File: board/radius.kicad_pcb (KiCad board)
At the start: 2 copper layers, 25.4 x 12.1 mm, 11 parts, among them IC1 STM8S003F3P, P1 CONN_01X04, P2 CONN_01X10, U1 CH340G, U2 LM2931AZ-3.3/5.0, Y1 Crystal

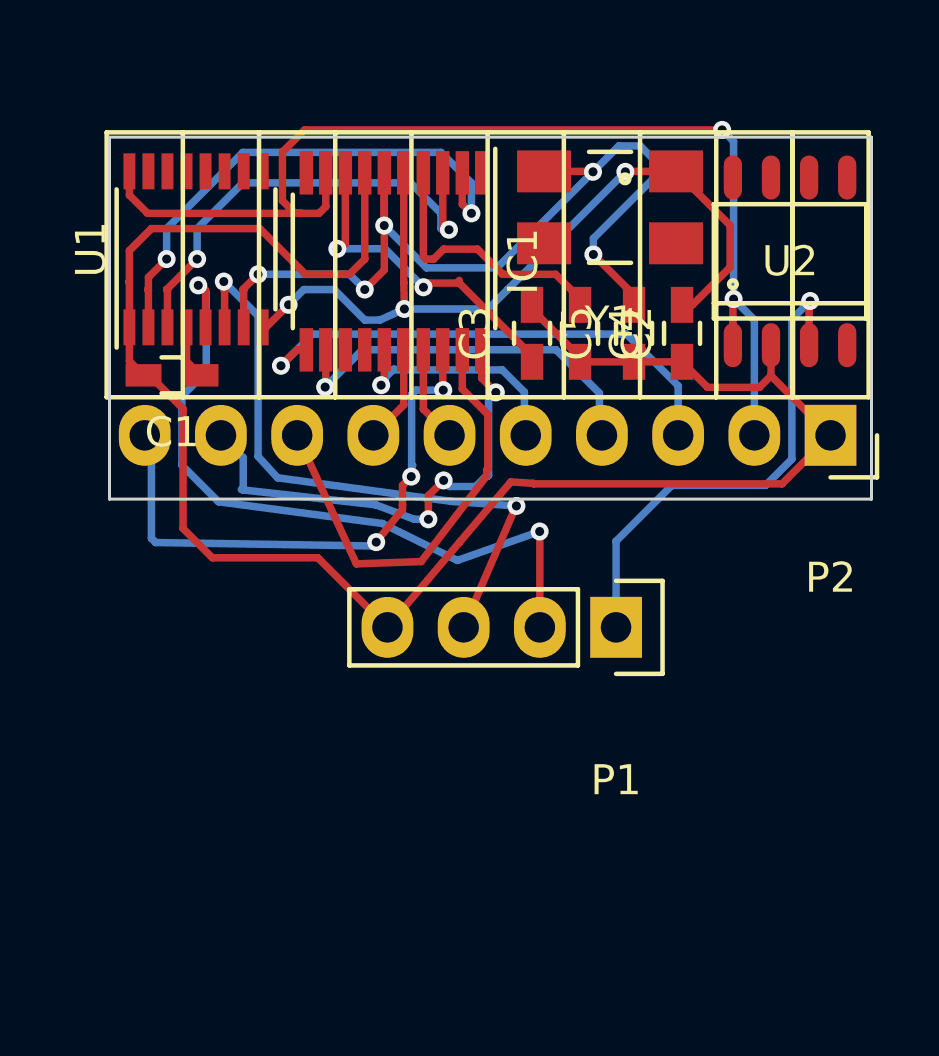
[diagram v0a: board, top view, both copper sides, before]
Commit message: Cleans up upper components.
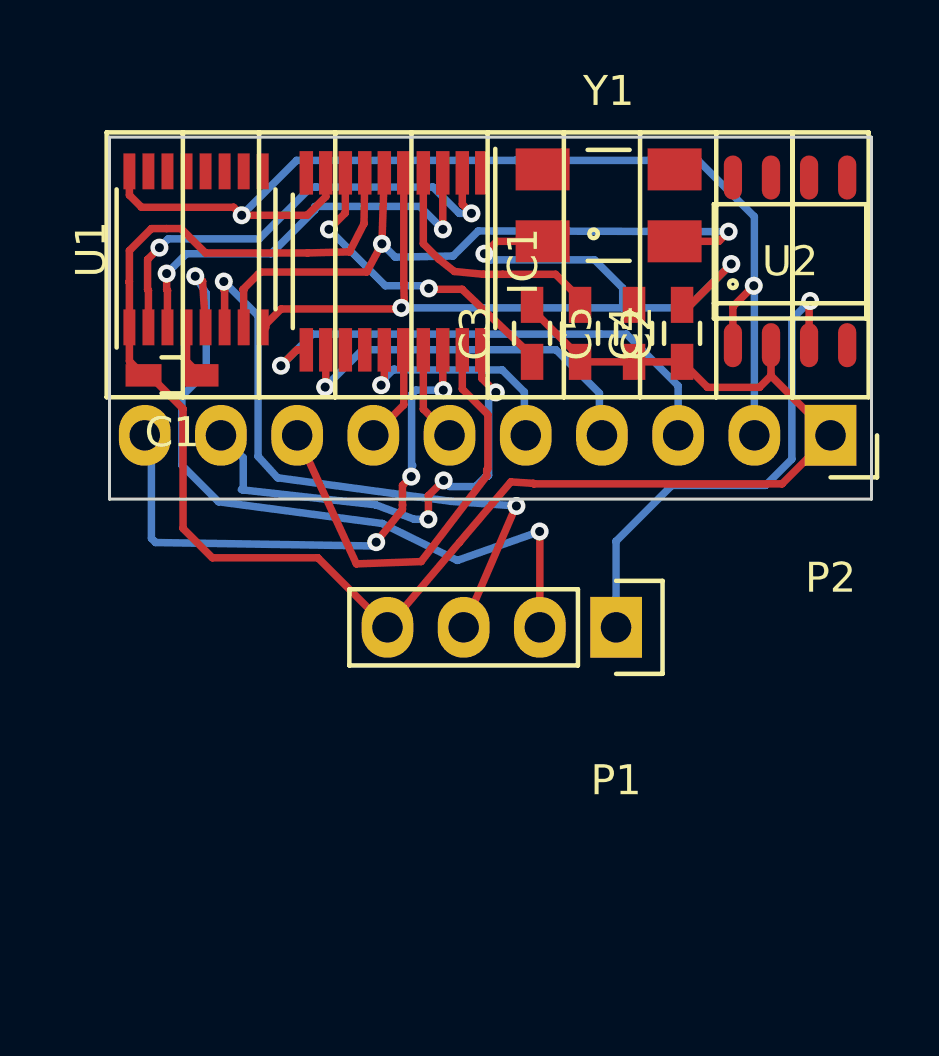
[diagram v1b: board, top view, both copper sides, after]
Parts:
- moved Y1 0.08 mm to (149.4, 101.3), turned to 0 degrees
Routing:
- net XI: track 31.1 -> 23.4 mm, vias 5 -> 2
- net XO: track 27.3 -> 31.4 mm
- net USB_TX: track 17.7 -> 15.9 mm
- net USB_RX: track 15.8 -> 14.2 mm
- net GND: track 61.1 -> 59.9 mm
- net VCC: track 39.1 -> 38.0 mm
- net Net-(C2-Pad1): track 9.20 -> 8.52 mm
- net D+: track 24.2 -> 24.8 mm

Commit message: Qualifying layout
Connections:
- IC1 pad 14: Net-(IC1-Pad14) -> G3
- IC1 pad 18: G3 -> Net-(IC1-Pad18)
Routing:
- net G3: track 19.0 -> 12.7 mm, vias 3 -> 1
- net D-: track 21.2 -> 16.7 mm
- net D+: track 24.8 -> 20.3 mm, vias 2 -> 1
- net TXD: track 15.0 -> 18.7 mm, vias 0 -> 3
- net XI: track 23.4 -> 26.4 mm
- net XO: track 31.4 -> 29.3 mm, vias 3 -> 4
- net SDA: track 17.1 -> 19.1 mm
- net Net-(C3-Pad1): track 10.8 -> 12.6 mm
- net SCK: track 8.09 -> 9.02 mm
- net SCL: track 12.9 -> 13.6 mm
- net GND: track 59.9 -> 60.6 mm
- net USB_TX: track 15.9 -> 16.6 mm
- net USB_RX: track 14.2 -> 14.8 mm
- net RXD: track 16.5 -> 16.4 mm, vias 3 -> 1

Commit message: Redone
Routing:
- net TXD: track 18.7 -> 14.0 mm, vias 3 -> 1
- net VCC: track 38.0 -> 42.1 mm
- net G3: track 12.7 -> 14.9 mm
- net SCK: track 9.02 -> 7.15 mm
- net XO: track 29.3 -> 27.5 mm
- net D-: track 16.7 -> 15.2 mm, vias 2 -> 0
- net SCL: track 13.6 -> 15.0 mm
- net RXD: track 16.4 -> 15.2 mm
- net USB_TX: track 16.6 -> 15.6 mm
- net D+: track 20.3 -> 19.7 mm
- net GND: track 60.6 -> 60.1 mm, vias 0 -> 1
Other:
- board size 25.4 x 12.1 mm -> 25.4 x 28.6 mm

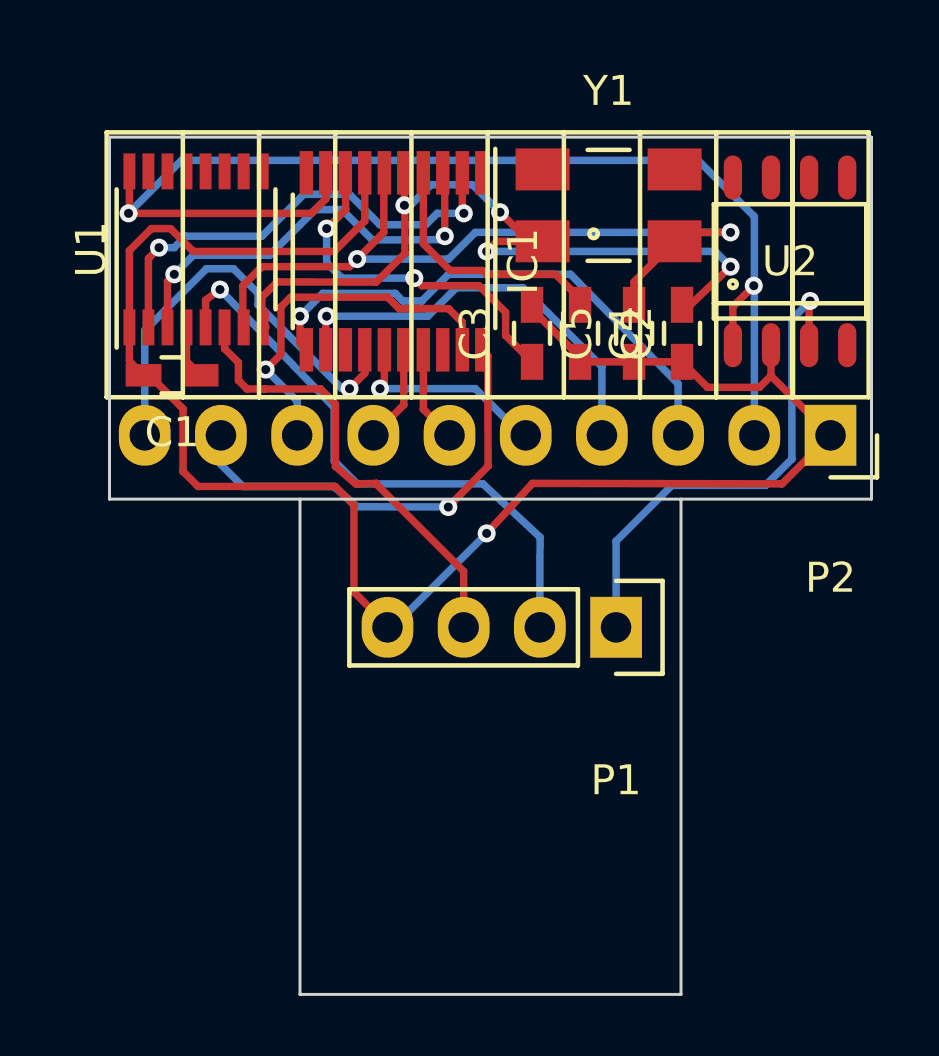
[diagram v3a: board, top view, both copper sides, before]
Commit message: Tighest layout
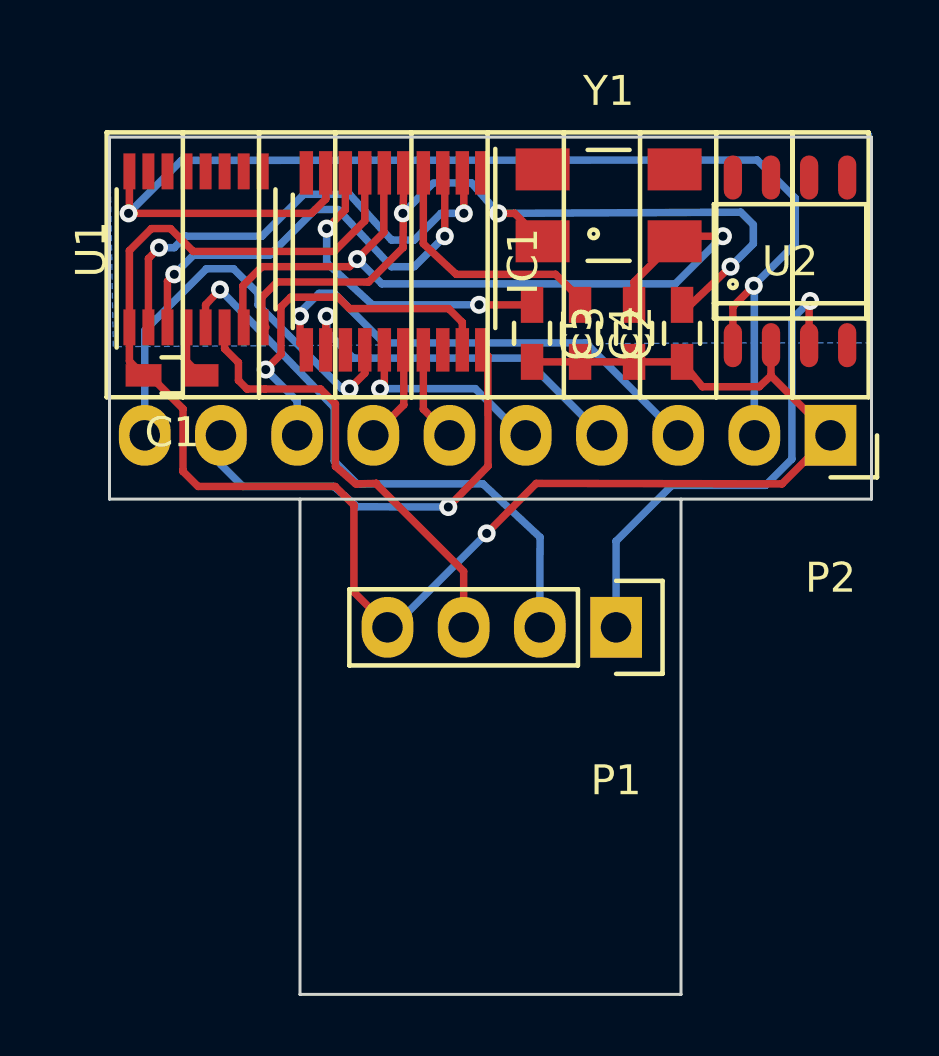
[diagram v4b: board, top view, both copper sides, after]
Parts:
- turned C3 to 270 degrees
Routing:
- net SCL: track 15.0 -> 12.4 mm
- net SDA: track 18.9 -> 16.3 mm
- net Net-(C3-Pad1): track 12.2 -> 10.7 mm
- net VCC: track 42.1 -> 43.3 mm
- net USB_RX: track 14.4 -> 15.2 mm
- net XO: track 27.5 -> 27.8 mm, vias 4 -> 3
- added copper zone on B.Cu, net VCC
